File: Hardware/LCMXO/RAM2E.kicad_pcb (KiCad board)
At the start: 4 copper layers, 78.2 x 50 mm, 64 parts, among them J1 AppleIIeAux, J2 JTAG, J3 C14M, U1 LCMXO256-TN100, U11 25F010, U2 W9812G6KH-6, U3 74LVC245APW, U4 74LVC245APW, U5 74LVC245APW, U6 74AHCT245PW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

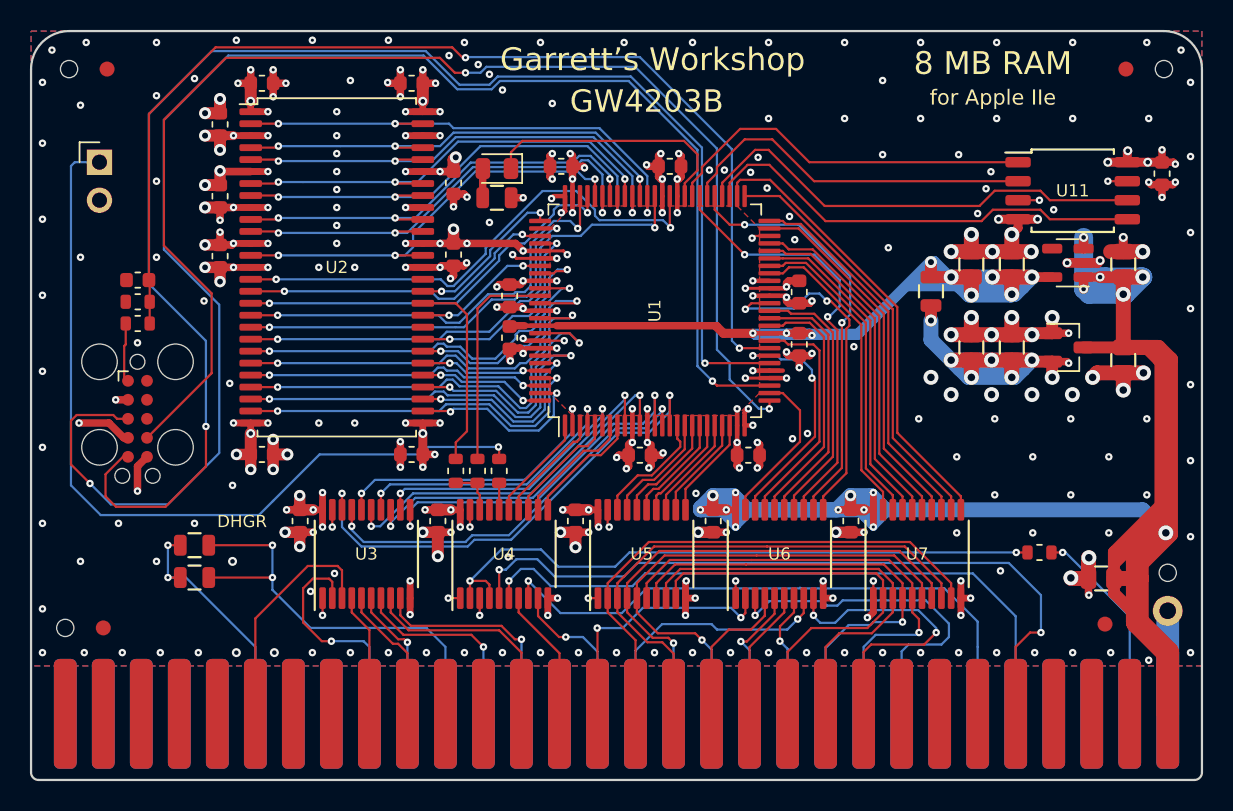
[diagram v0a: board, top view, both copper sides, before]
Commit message: Fixed MachXO board wrong JTAG pinout
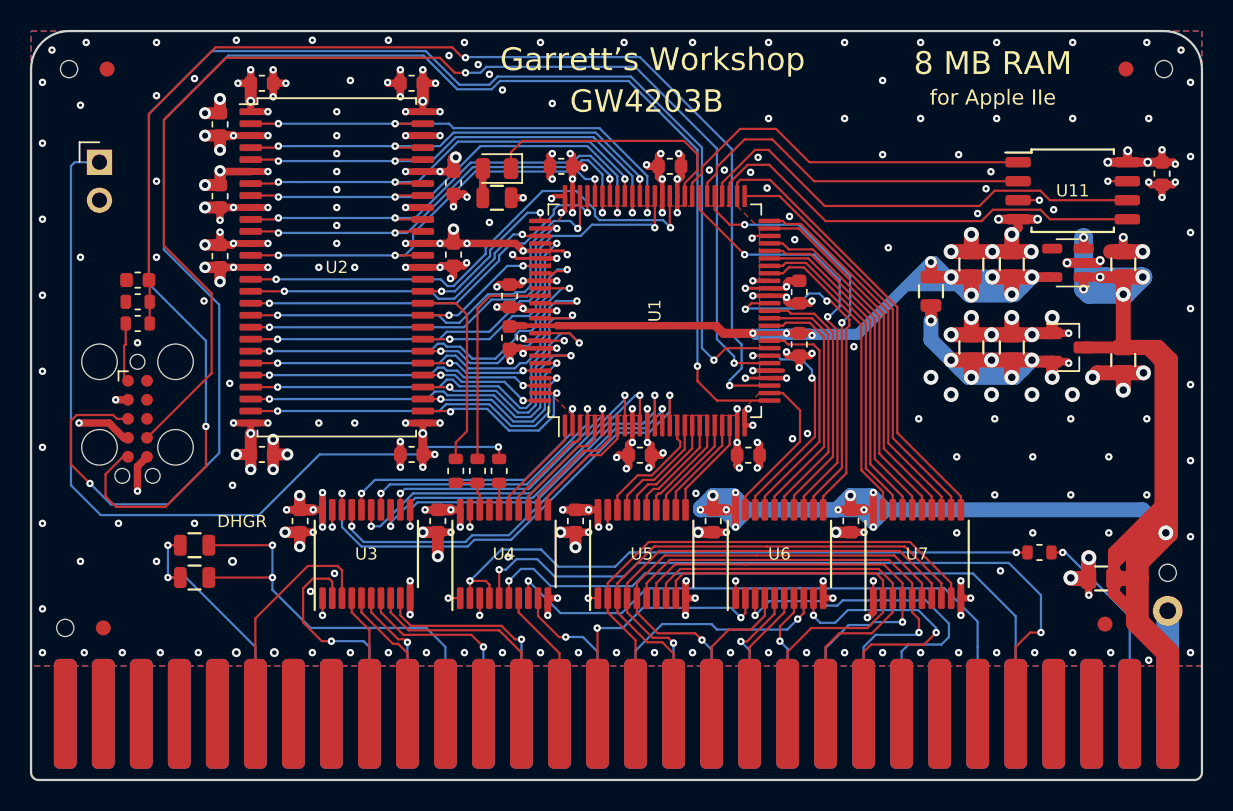
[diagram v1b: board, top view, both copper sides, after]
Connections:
- net /D~OE~ renamed /D~{OE}
- net /R~W~ renamed /R~{W}
- net /R~W~80 renamed /R~{W}80
- net /R~W~80in renamed /R~{W}80in
- net /R~W~in renamed /R~{W}in
- net /S~CS~ renamed /S~{CS}
- net /V~OE~ renamed /V~{OE}
- net /~80VID~ renamed /~{80VID}
- net /~ALTVID~ renamed /~{ALTVID}
- net /~C07X~ renamed /~{C07X}
- net /~C07X~in renamed /~{C07X}in
- net /~CASEN~ renamed /~{CASEN}
- net /~CAS~ renamed /~{CAS}
- net /~CLRGAT~ renamed /~{CLRGAT}
- net /~CS~ renamed /~{CS}
- net /~EN80~ renamed /~{EN80}
- net /~EN80~in renamed /~{EN80}in
- net /~ENTMG~ renamed /~{ENTMG}
- net /~ENVID~ renamed /~{ENVID}
- net /~FRCTXT~ renamed /~{FRCTXT}
- net /~LDPS~ renamed /~{LDPS}
- net /~PCAS~ renamed /~{PCAS}
- net /~PRAS~ renamed /~{PRAS}
- net /~RA10~ renamed /~{RA10}
- net /~RA9~ renamed /~{RA9}
- net /~RAS~ renamed /~{RAS}
- net /~SEROUT~ renamed /~{SEROUT}
- net /~SYNC~ renamed /~{SYNC}
- net /~WE~ renamed /~{WE}
- net /~WNDW~ renamed /~{WNDW}
- J2 pad 10: Net-(J2-Pad10) -> unconnected-(J2-Pin_10-Pad10)
- J2 pad 8: Net-(J2-Pad8) -> unconnected-(J2-Pin_8-Pad8)
- J2 pad 9: Net-(J2-Pad9) -> unconnected-(J2-Pin_9-Pad9)
- U1 pad 26: /TDO -> /TMS
- U1 pad 28: /TMS -> /TCKr
- U1 pad 31: /TDI -> /TDO
- U1 pad 33: /TCKr -> /TDI
- U4 pad 17: Net-(U4-Pad17) -> unconnected-(U4-B1-Pad17)
- U9 pad 4: Net-(U9-Pad4) -> unconnected-(U9-NC-Pad4)
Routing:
- net /TCKr: track 73.2 -> 76.7 mm
- net /TDO: track 85.7 -> 83.0 mm
- net /TMS: track 103.6 -> 104.6 mm
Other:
- net class Default removed
